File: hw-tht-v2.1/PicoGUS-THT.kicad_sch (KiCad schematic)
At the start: 68 parts, among them J1 Bus_ISA_8bit, J10 RUN, J2 SWD, J3 IRQ/DMA, J4 UART_TX, J5 USB-A host, J6 USB-C program, J7 SJ1-3535NG, J8 Waveblaster, J9 SJ1-3535NG-GR, SW1 BOOTSEL, U1 SN74CB3T3257, U12 Core2350B, U13 M62429L, U2 SN74CB3T3257, U3 74AHC14, U4 74AHC00, U5 74AHC00, U6 74AHCT126, U7 74AHC244, U8 APS6404L-3SQR-SN, U9 MCP1826S-3302E/AB

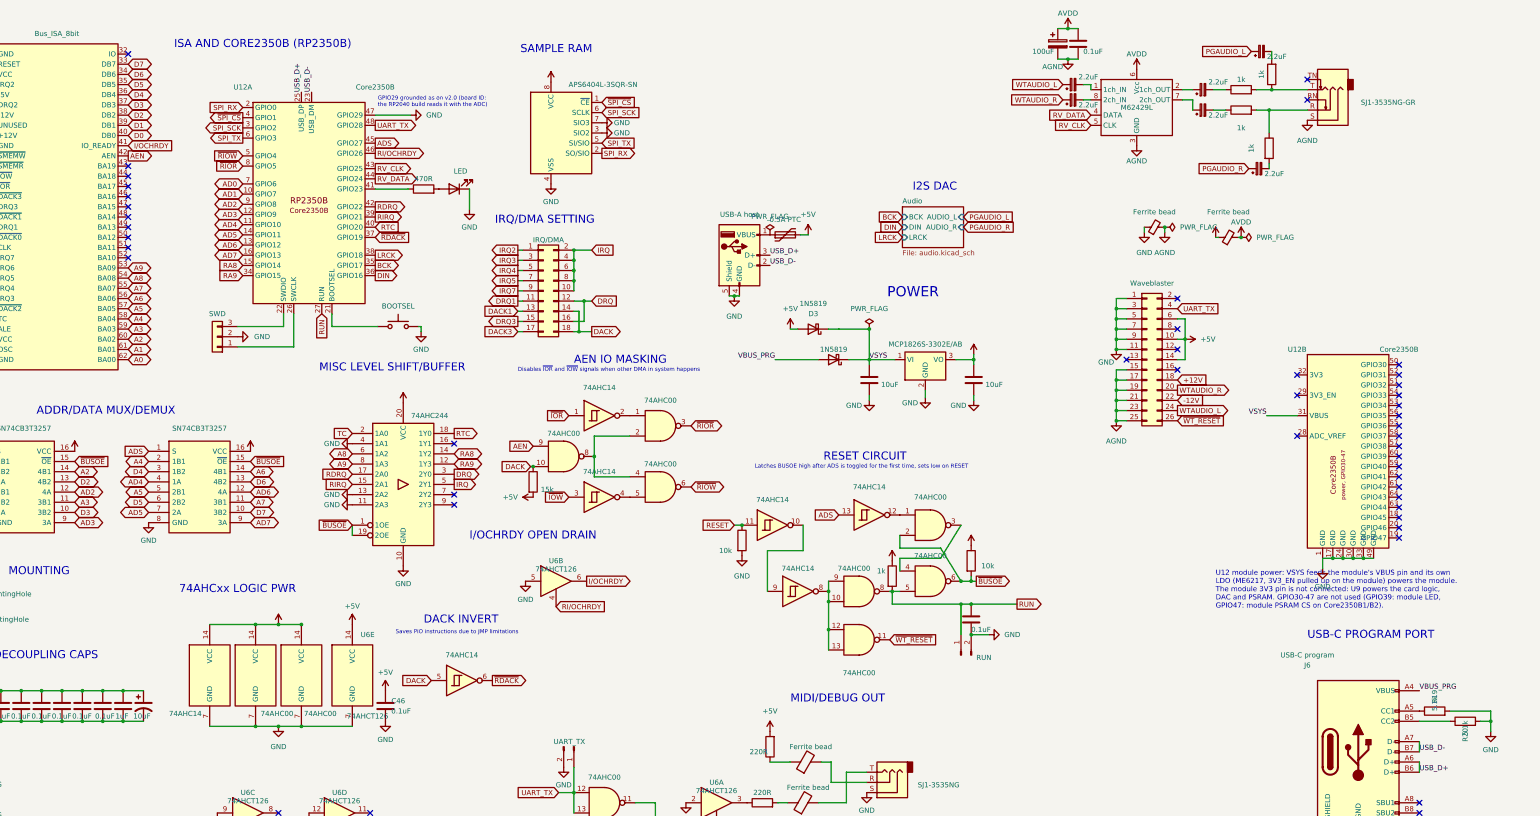
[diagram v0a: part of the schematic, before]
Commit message: THT v2.1: THT BOM, THT v1.3 op-amp mixer, module PSRAM, placed board
Milestone 1 of the through-hole v2.1 board.

Schematic:
- Line-out mixer from the THT v1.3 boards on a new sheet (mixer.kicad_sch):
  U11 NE5532 inverting summing amplifier on ISA +/-12V (10R/47uF filters),
  Waveblaster through 10k (+6 dB) after v2.0's M62429 volume, PCM through
  20k DC coupled, 20k || 47pF C0G feedback, 100R outputs, 100k pull-downs
  at the Waveblaster inputs. Replaces v2.0's passive 1k mix (R6-R9) and the
  DAC coupling caps C43/C44. Wired through sheet pins where R6-R9 were.
- U8 (APS6404L, PIO SPI on GPIO0-3) removed: the GUS sample RAM is the
  Core2350B2's 8 MB PSRAM on the RP2350B QMI (CS1 = GPIO47). GPIO0-3 now
  carry no-connect flags; C8/C9 removed. Needs the firmware port.
- C39-C42 are 2.2 uF film coupling caps (non-polar symbol).
- ERC: 0 errors. Netlist checked against v2.0 transformed by these changes.

BOM (BOM-THT.csv): THT status per line (THT / different THT part / no THT
version exists / module), the v2.0 part each line replaces, DigiKey and
LCSC numbers, alternatives, kit items and the v2.0 parts that are gone.
No through-hole version exists for: RP2040 + flash + crystal (module),
APS6404L (module PSRAM), SN74CB3T3257 and PCM5100A (TSSOP on DIP
adapters), M62429 (SOP-8 on a DIP-8 adapter). Audio parts: polyester
film couplings (TDK B32529 / Faratronic C241; new dual footprint also
takes a 5 mm bipolar electrolytic), C0G filter and feedback caps,
Panasonic FR AVDD bulk, NE5532 with OPA2134PA as the upgrade.

Board: placed (not routed) with the mixer above J9; DRC with schematic
parity clean apart from unrouted connections. CUI jack models as v1.3.2.
README updated; first front render and schematic PDF.

Co-Authored-By: Claude Opus 5.5 <noreply@anthropic.com>
Claude-Session: https://claude.ai/code/session_013W5uqvghZgJXEB5tgmrp98
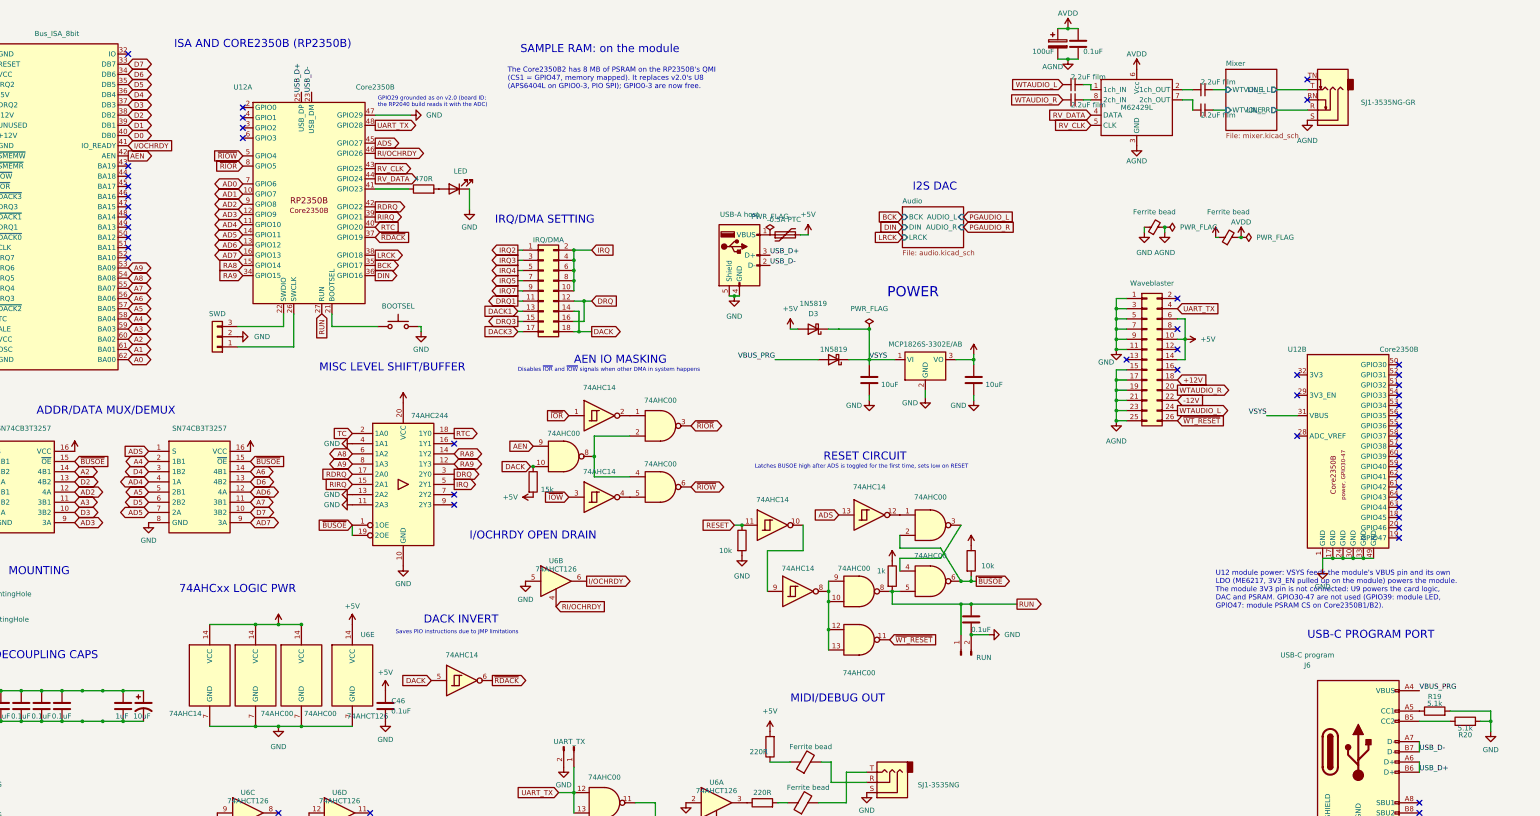
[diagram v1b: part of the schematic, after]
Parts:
- removed C43, C44: 2.2uF, Capacitor_THT:CP_Radial_D5.0mm_P2.00mm, symbol Device:C_Polarized_Small
- removed C8, C9: 0.1uF, Capacitor_THT:C_Disc_D5.0mm_W2.5mm_P5.00mm, symbol Device:C
- removed R6, R7, R8, R9: 1k, Resistor_THT:R_Axial_DIN0207_L6.3mm_D2.5mm_P10.16mm_Horizontal, symbol Device:R
- removed U8: APS6404L-3SQR-SN, PiGUS library:DIP-8_W7.62mm_SOIC-8_Adapter, symbol Memory_RAM:ESP-PSRAM32
- C38: DigiKey 1572-1658-ND -> P14391-ND; LCSC C108735 (Rubycon 16YXJ100M5X11) -> C439880 (Rubycon 16ZLH100MEFC5X11); MPN 107CKS016M -> EEU-FR1C101; Manufacturer Cornell Dubilier -> Panasonic
- C39, C40, C41, C42: value 2.2uF -> 2.2uF film; footprint Capacitor_THT:CP_Radial_D5.0mm_P2.00mm -> PiGUS library:C_Film_P5.00mm_7.8x7.8mm_or_CP_D5.0mm_P2.00mm; symbol Device:C_Polarized_Small -> Device:C_Small; DigiKey 1572-1376-ND -> 495-1127-ND; LCSC C112511 (AISHI ERS1HM2R2D11OT) -> C5372007 (Faratronic C241J225J2SC000); MPN 225CKH050M -> B32529D0225J000; Manufacturer Cornell Dubilier -> TDK
- J5: DigiKey (none) -> not stocked: LCSC only; LCSC (none) -> C2345; Manufacturer CNC Tech -> Jing Extension of the Electronic Co.
- R19, R20: DigiKey 5.10KXBK-ND -> MFR-25FBF52-5K1-ND; LCSC C1500210 (UNI-ROYAL MFR0W4F5101A50) -> C1369975
- U13: DigiKey 2156-M62429FP#CF0J-ND (Renesas M62429FP, 4.5-5.5V) -> not stocked: LCSC only (DigiKey marketplace 2156-M62429FP#C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
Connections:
- net Mixer/LINE_L: now reaches J9.T
- net Mixer/WTVOL_L: now reaches C41.2
- net Mixer/LINE_R: now reaches J9.R
- net Mixer/WTVOL_R: now reaches C42.2
- net SPI_RX: no longer names the net of U12.2 (GPIO0)
- net SPI_SCK: no longer names the net of U12.3 (GPIO2)
- net SPI_TX: no longer names the net of U12.6 (GPIO3)
- net ~{SPI_CS}: no longer names the net of U12.4 (GPIO1)
- no-connect marks 57 -> 61
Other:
- added sheet Mixer (mixer.kicad_sch)
- note added: "SAMPLE RAM: on the module"
- note added: "The Core2350B2 has 8 MB of PSRAM on the RP2350B's QMI (CS1 = GPIO47, memory mapped). It replaces v2.0's U8 (APS6404L on GPIO0-3, PIO SPI); GPIO0-3 are now free."
- note removed: "SAMPLE RAM"
